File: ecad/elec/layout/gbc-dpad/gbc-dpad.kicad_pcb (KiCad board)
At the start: 2 copper layers, 9 parts

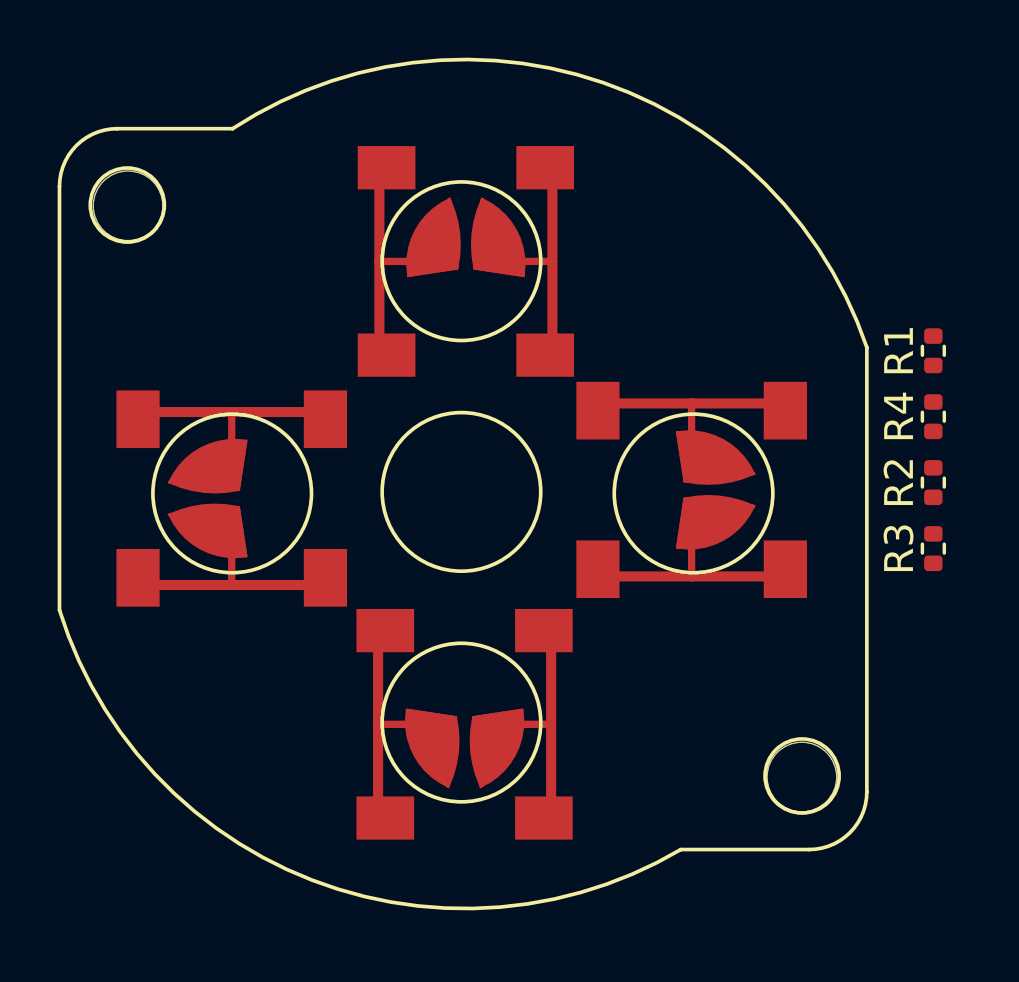
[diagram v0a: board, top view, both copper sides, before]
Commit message: Fix/atopile ecad (#82)
* fix(ecad): Fix bugs in atopile version of the design
* Add missing pullup resistors to AW9523 RSTN and INTN lines
* Fix I/O configuration for AW9523 so that all the inputs go to the same port pins as the previous version of the electronics

* minor cleanup to box3 after update to at 0.2.58

* fix udpate max17038 pullup to properly go to alert line after other fix

* typo

* update layout

* minor update to layout

* fix(buttons): pulldown -> pullup (so they are active low)

* update buttons to be pullup instead of pulldown; change led to be powered off VBUS instead of vbat

* update button footprints - start/select better aligned and all buttons have extra wires to ensure connections

* add net names and ensure packages are specified

* update box-emu-base layout

* update box-emu and box-3-emu layouts

* udpate to kicad 8

* add net name overrides and update all boards

* update atopile action to kicad 8

* comment out blender render
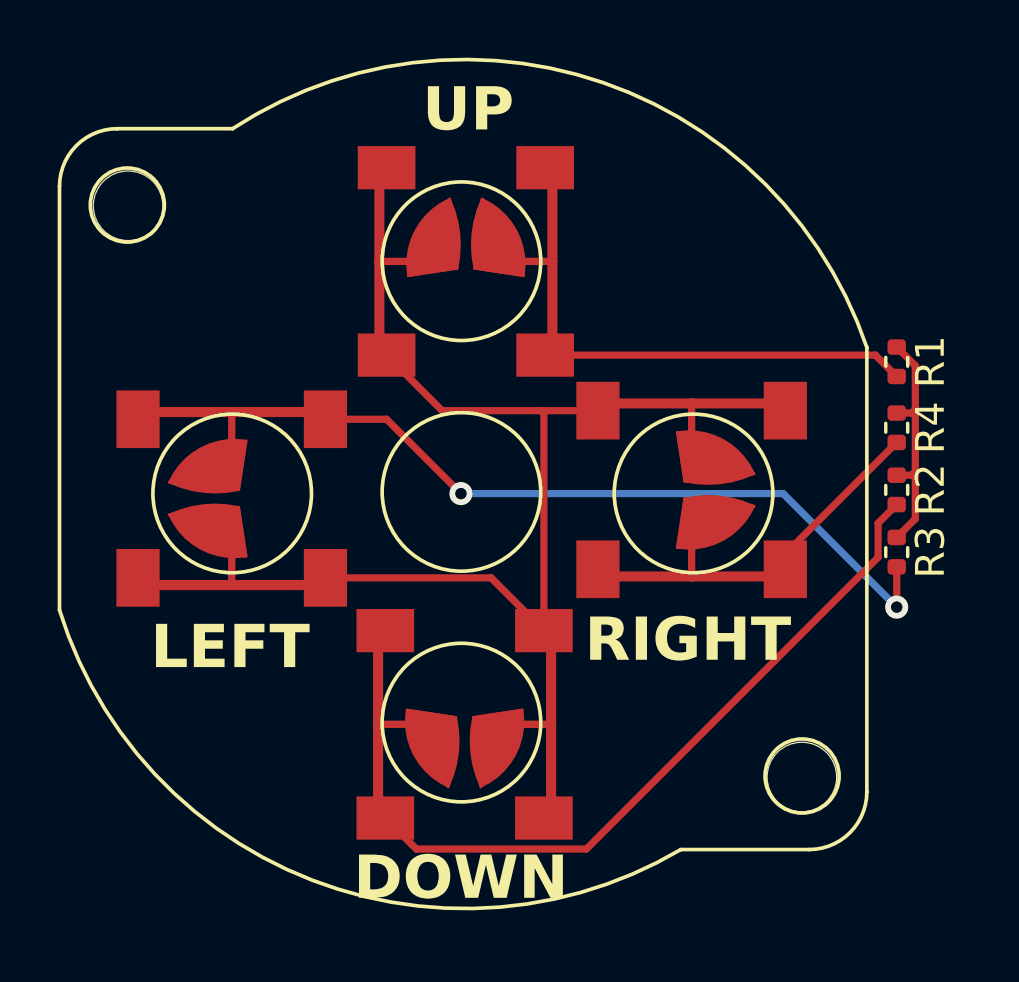
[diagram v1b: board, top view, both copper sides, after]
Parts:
- moved R4 1.33 mm to (166.4, 73.5), turned to -90 degrees
- moved R1 1.33 mm to (166.4, 71.2), turned to -90 degrees
- moved R2 1.30 mm to (166.4, 75.7), turned to -90 degrees
- moved R3 1.28 mm to (166.4, 77.8), turned to -90 degrees
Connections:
- R1 pad 1: gnd -> vcc
- R2 pad 1: gnd -> vcc
- R3 pad 1: gnd -> vcc
- R4 pad 1: gnd -> vcc
- U2 pad 2: vcc -> gnd
- U2 pad 4: vcc -> gnd
- U3 pad 2: vcc -> gnd
- U3 pad 4: vcc -> gnd
- U4 pad 2: vcc -> gnd
- U4 pad 4: vcc -> gnd
- U5 pad 2: vcc -> gnd
- U5 pad 4: vcc -> gnd
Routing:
- net gnd: track 0.00 -> 51.0 mm
- net left: track 0.00 -> 30.6 mm, vias 0 -> 2
- net down: track 0.00 -> 30.5 mm
- net up: track 0.00 -> 19.2 mm
- net right: track 0.00 -> 12.7 mm
- net vcc: track 0.00 -> 8.53 mm
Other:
- board text added: "DOWN"
- board text added: "LEFT"
- board text added: "RIGHT"
- board text added: "UP"
